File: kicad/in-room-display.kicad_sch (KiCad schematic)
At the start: 3 parts, among them J1 USBCpow, J2 Display, U1 ESP32-DevKitC

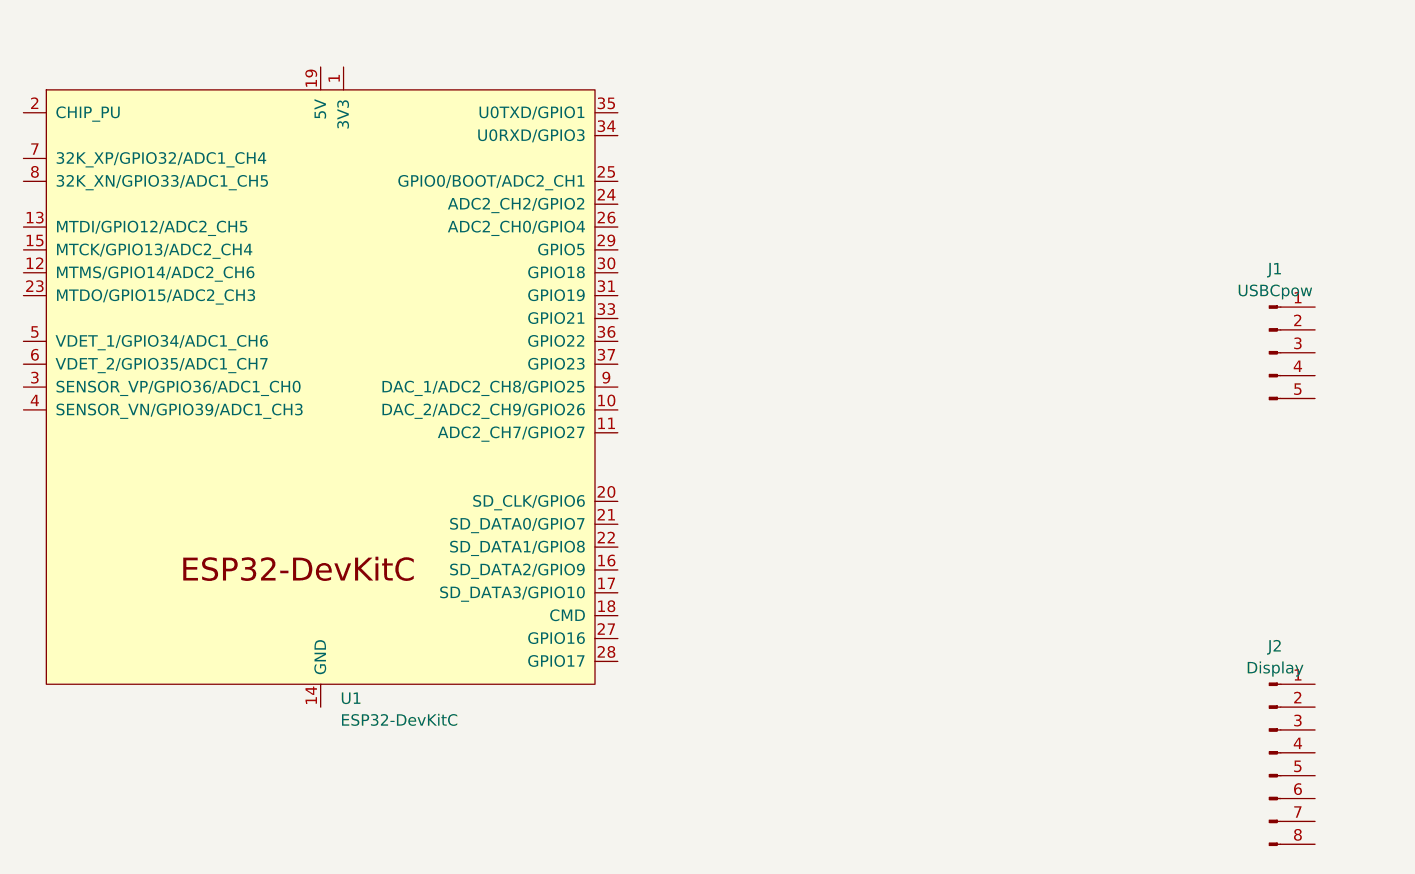
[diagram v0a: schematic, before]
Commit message: create schematic for ST7789
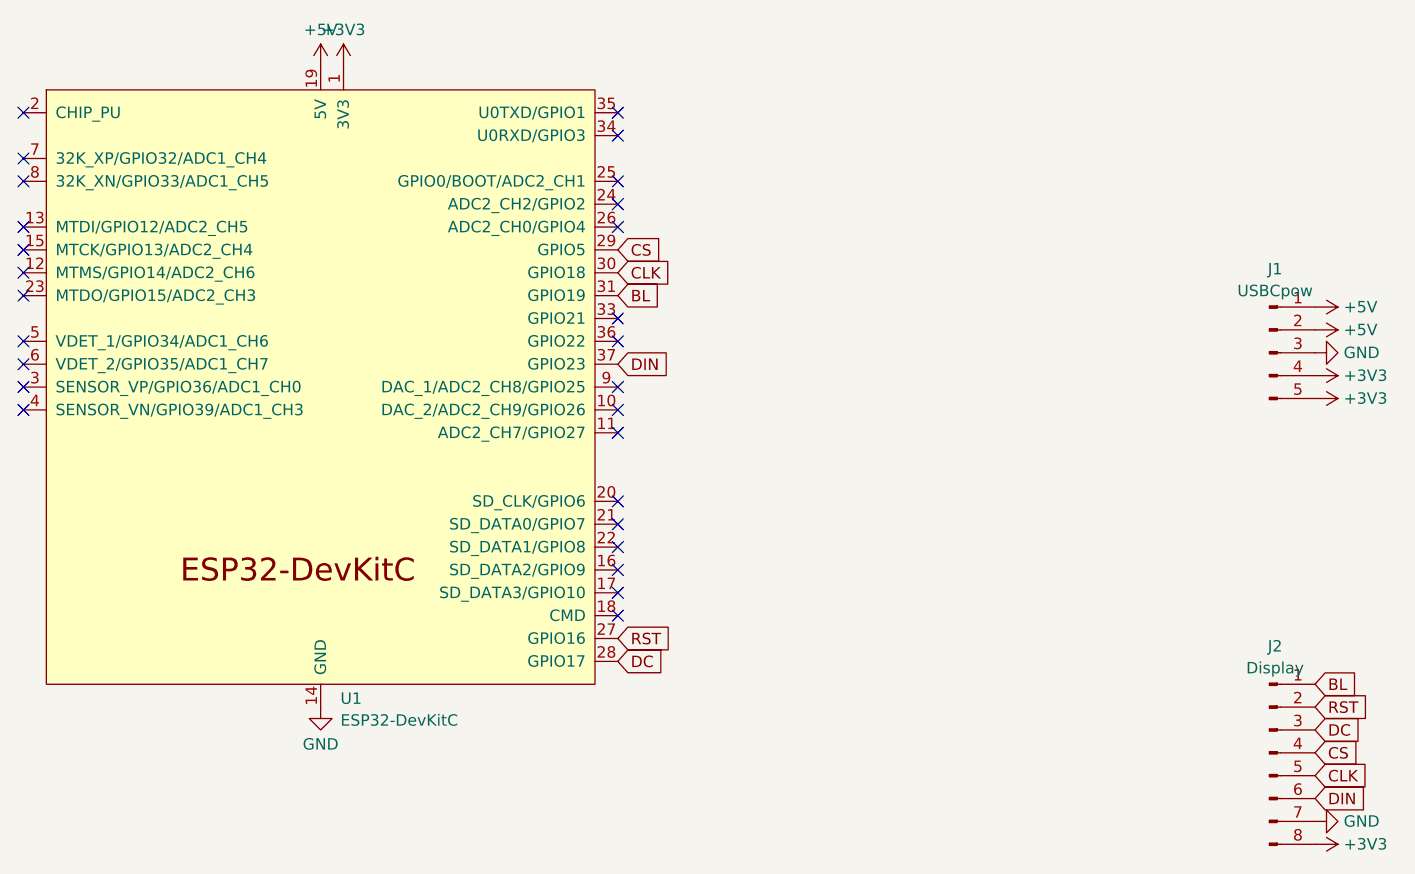
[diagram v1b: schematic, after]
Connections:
- net BL: now reaches J2.1 (Pin_1)
- net BL: now also U1.31 (GPIO19)
- net RST: now reaches J2.2 (Pin_2)
- net RST: now also U1.27 (GPIO16)
- net DC: now reaches J2.3 (Pin_3)
- net DC: now also U1.28 (GPIO17)
- net CS: now reaches J2.4 (Pin_4)
- net CS: now also U1.29 (GPIO5)
- net CLK: now reaches J2.5 (Pin_5)
- net CLK: now also U1.30 (GPIO18)
- net DIN: now reaches J2.6 (Pin_6)
- net DIN: now also U1.37 (GPIO23)
- net GND: now reaches J2.7 (Pin_7)
- net GND: now also J1.3 (Pin_3), U1.14 (GND), U1.32 (GND), U1.38 (GND)
- net +3V3: now reaches J2.8 (Pin_8)
- net +3V3: now also J1.4 (Pin_4), J1.5 (Pin_5), U1.1 (3V3)
- net +5V: now reaches J1.1 (Pin_1)
- net +5V: now also J1.2 (Pin_2), U1.19 (5V)
- no-connect marks 0 -> 27
